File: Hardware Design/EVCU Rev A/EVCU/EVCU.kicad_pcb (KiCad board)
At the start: 4 copper layers, 60 parts, among them J1 Conn_01x06, J4 Micro_SD_Card, U1 AZ1084-3.3, U10 EMIF06-MSD02N16, U11 ESDALC6V1W5, U2 AP62250WU-7, U3 STM32L4R9ZITx, U5 MPU-6500, U6 SN65HVD230, U9 ESDCAN24-2BLY, X1 ECS-2520MV-160-CN-TR

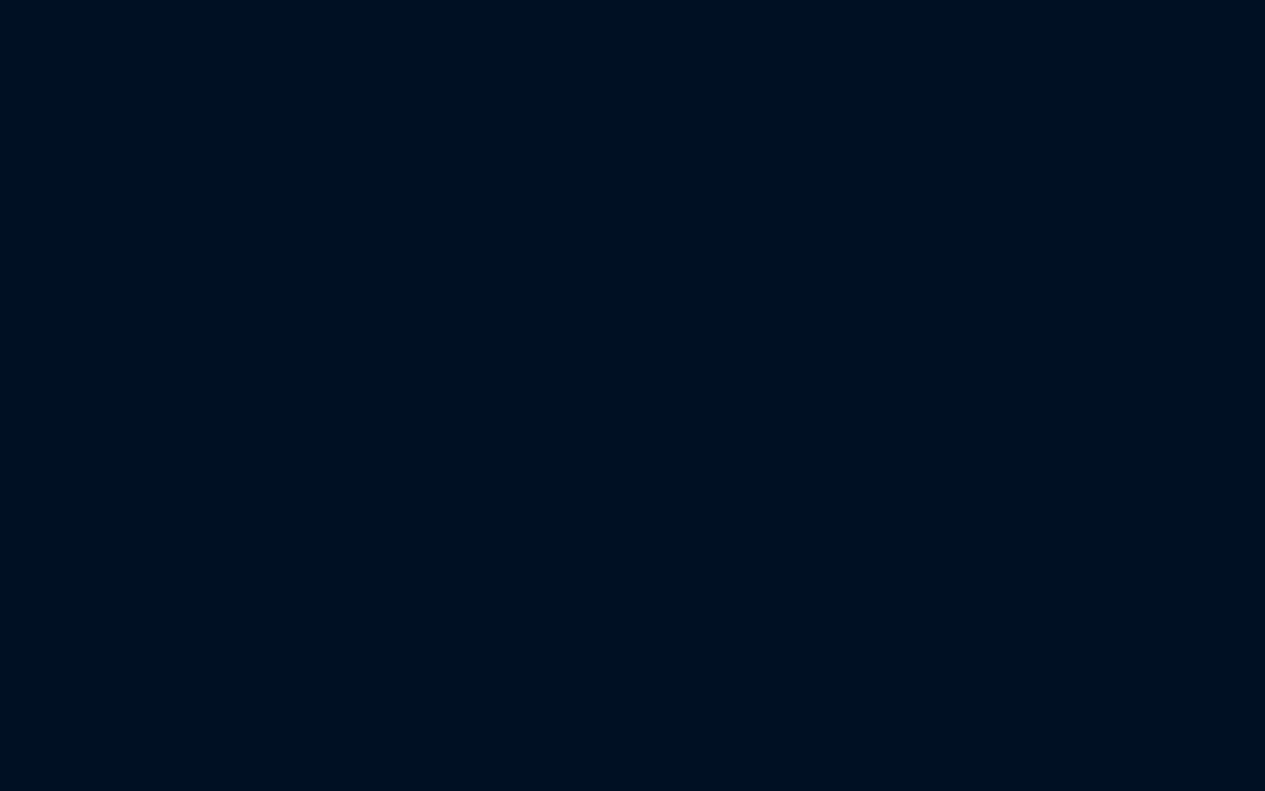
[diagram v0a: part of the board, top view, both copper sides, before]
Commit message: cap 1206 change, fuse, lin reg to 1117, testpoints, bom additions
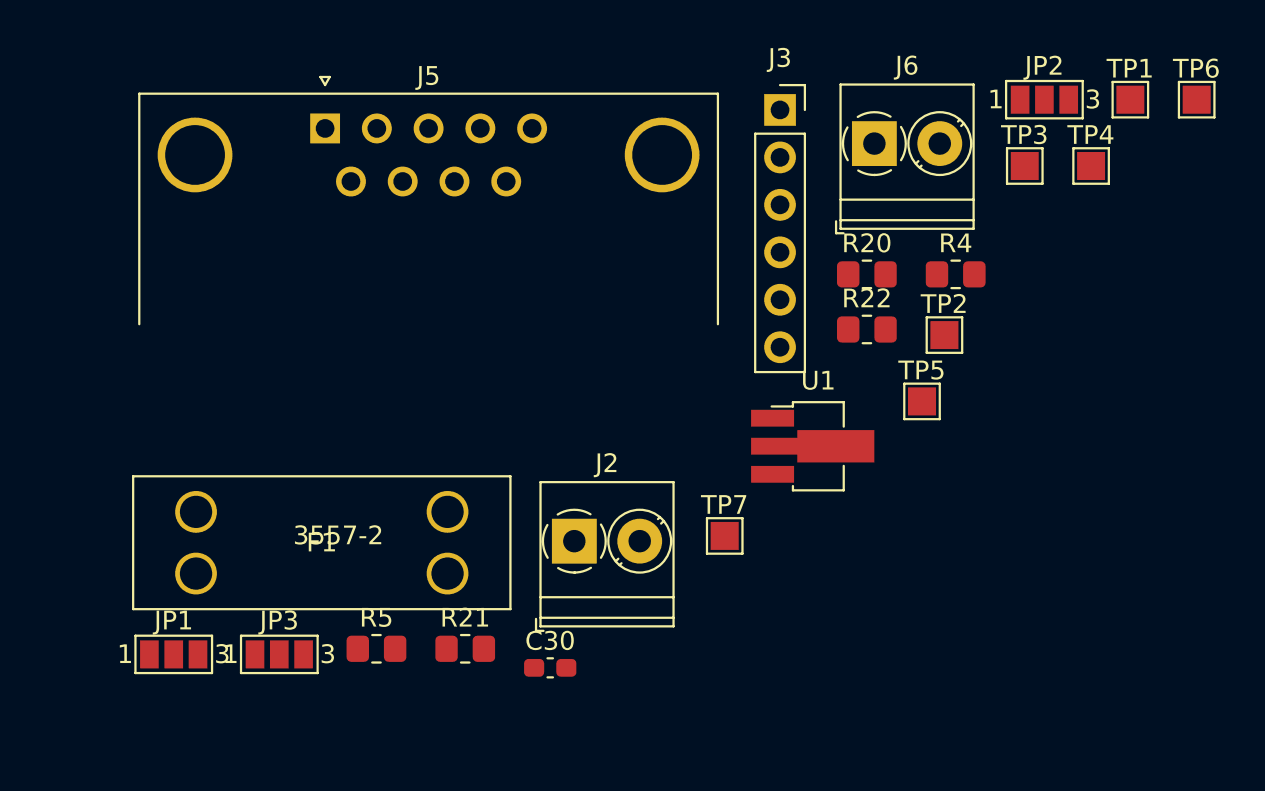
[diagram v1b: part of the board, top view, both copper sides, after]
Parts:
- added C30: 0.1uF, Capacitor_SMD:C_0603_1608Metric_Pad1.08x0.95mm_HandSolder, F.Cu at (188.3, 92.4)
- added F1: 3557-2, 3557-2:3557-2, F.Cu at (169.4, 84.1)
- added J2: Conn_01x02, TerminalBlock_Phoenix:TerminalBlock_Phoenix_PT-1,5-2-3.5-H_1x02_P3.50mm_Horizontal, F.Cu at (189.6, 85.6)
- added J3: APPS/BSE_Conn, Connector_PinSocket_2.54mm:PinSocket_1x06_P2.54mm_Vertical, F.Cu at (200.6, 62.5)
- added J5: DB9_Male, Connector_Dsub:DSUB-9_Male_Horizontal_P2.77x2.84mm_EdgePinOffset7.70mm_Housed_MountingHolesOffset9.12mm, F.Cu at (176.3, 63.5)
- added J6: Conn_01x02, TerminalBlock_Phoenix:TerminalBlock_Phoenix_PT-1,5-2-3.5-H_1x02_P3.50mm_Horizontal, F.Cu at (205.7, 64.3)
- added JP1: SolderJumper_3_Open, Jumper:SolderJumper-3_P1.3mm_Open_Pad1.0x1.5mm_NumberLabels, F.Cu at (168.2, 91.7)
- added JP2: SolderJumper_3_Open, Jumper:SolderJumper-3_P1.3mm_Open_Pad1.0x1.5mm_NumberLabels, F.Cu at (214.8, 62.0)
- added JP3: SolderJumper_3_Open, Jumper:SolderJumper-3_P1.3mm_Open_Pad1.0x1.5mm_NumberLabels, F.Cu at (173.8, 91.7)
- added R20: 34kR, Resistor_SMD:R_0805_2012Metric_Pad1.20x1.40mm_HandSolder, F.Cu at (205.3, 71.3)
- added R21: 100kR, Resistor_SMD:R_0805_2012Metric_Pad1.20x1.40mm_HandSolder, F.Cu at (183.8, 91.4)
- added R22: 100kR, Resistor_SMD:R_0805_2012Metric_Pad1.20x1.40mm_HandSolder, F.Cu at (205.3, 74.3)
- added R4: 100kR, Resistor_SMD:R_0805_2012Metric_Pad1.20x1.40mm_HandSolder, F.Cu at (210.0, 71.3)
- added R5: 33kR, Resistor_SMD:R_0805_2012Metric_Pad1.20x1.40mm_HandSolder, F.Cu at (179.0, 91.4)
- added TP1: TestPoint_Probe, TestPoint:TestPoint_Pad_1.5x1.5mm, F.Cu at (219.4, 62.0)
- added TP2: TestPoint_Probe, TestPoint:TestPoint_Pad_1.5x1.5mm, F.Cu at (209.4, 74.6)
- added TP3: TestPoint_Probe, TestPoint:TestPoint_Pad_1.5x1.5mm, F.Cu at (213.7, 65.5)
- added TP4: TestPoint_Probe, TestPoint:TestPoint_Pad_1.5x1.5mm, F.Cu at (217.3, 65.5)
- added TP5: TestPoint_Probe, TestPoint:TestPoint_Pad_1.5x1.5mm, F.Cu at (208.2, 78.1)
- added TP6: TestPoint_Probe, TestPoint:TestPoint_Pad_1.5x1.5mm, F.Cu at (222.9, 62.0)
- added TP7: TestPoint_Probe, TestPoint:TestPoint_Pad_1.5x1.5mm, F.Cu at (197.7, 85.3)
- added U1: AZ1117-3.3, Package_TO_SOT_SMD:SOT-89-3_Handsoldering, F.Cu at (202.4, 80.5)
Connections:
- C25 pad 1: /VOUT_1_APPS -> Net-(C25-Pad1)
- C26 pad 1: /VOUT_2_APPS -> Net-(C26-Pad1)
- R8 pad 1: /VOUT_1_APPS -> Net-(C25-Pad1)
- R9 pad 1: /VOUT_2_APPS -> Net-(C26-Pad1)
- U2 pad 5: unconnected-(U2-Pad5) -> +BATT
- U3 pad 108: unconnected-(U3-Pad108) -> +3V3
- U3 pad 33: unconnected-(U3-Pad33) -> /VOUT_BSE

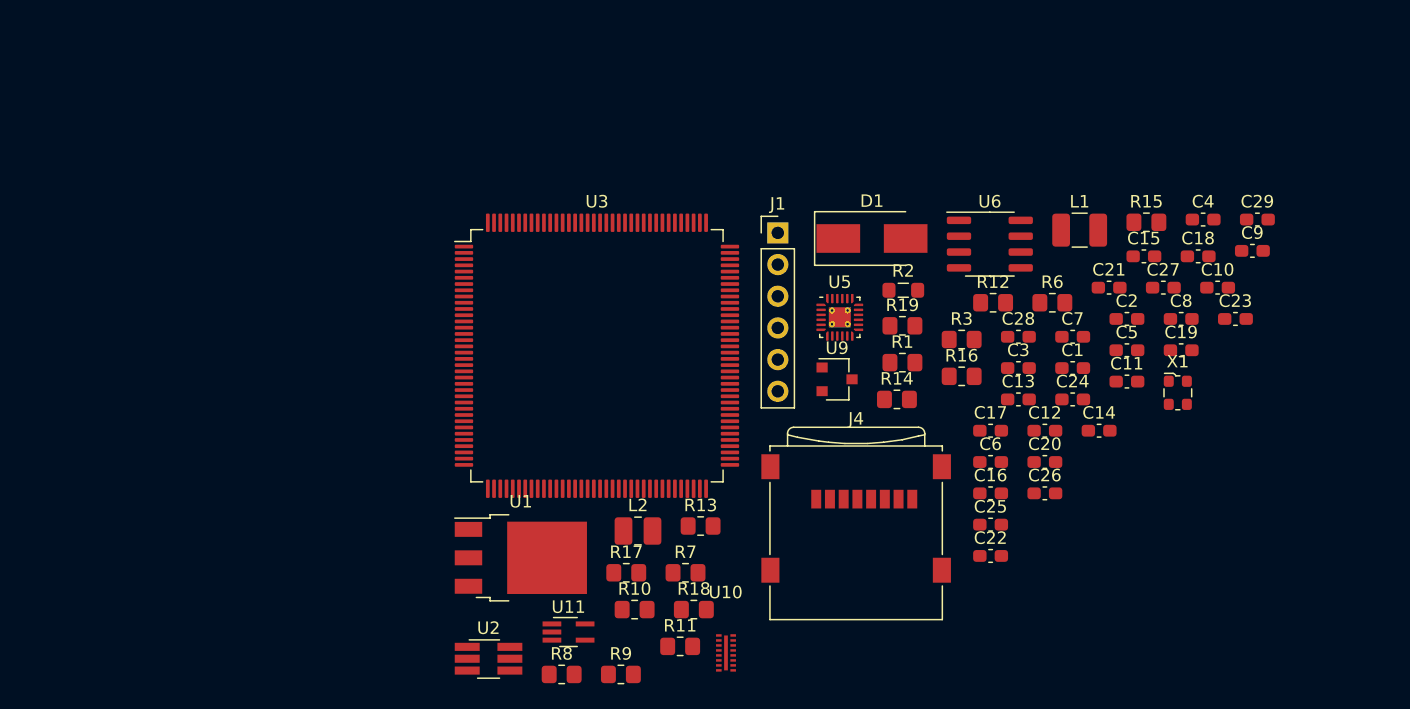
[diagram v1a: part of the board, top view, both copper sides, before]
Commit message: accelerometer layout and op-amp footprint
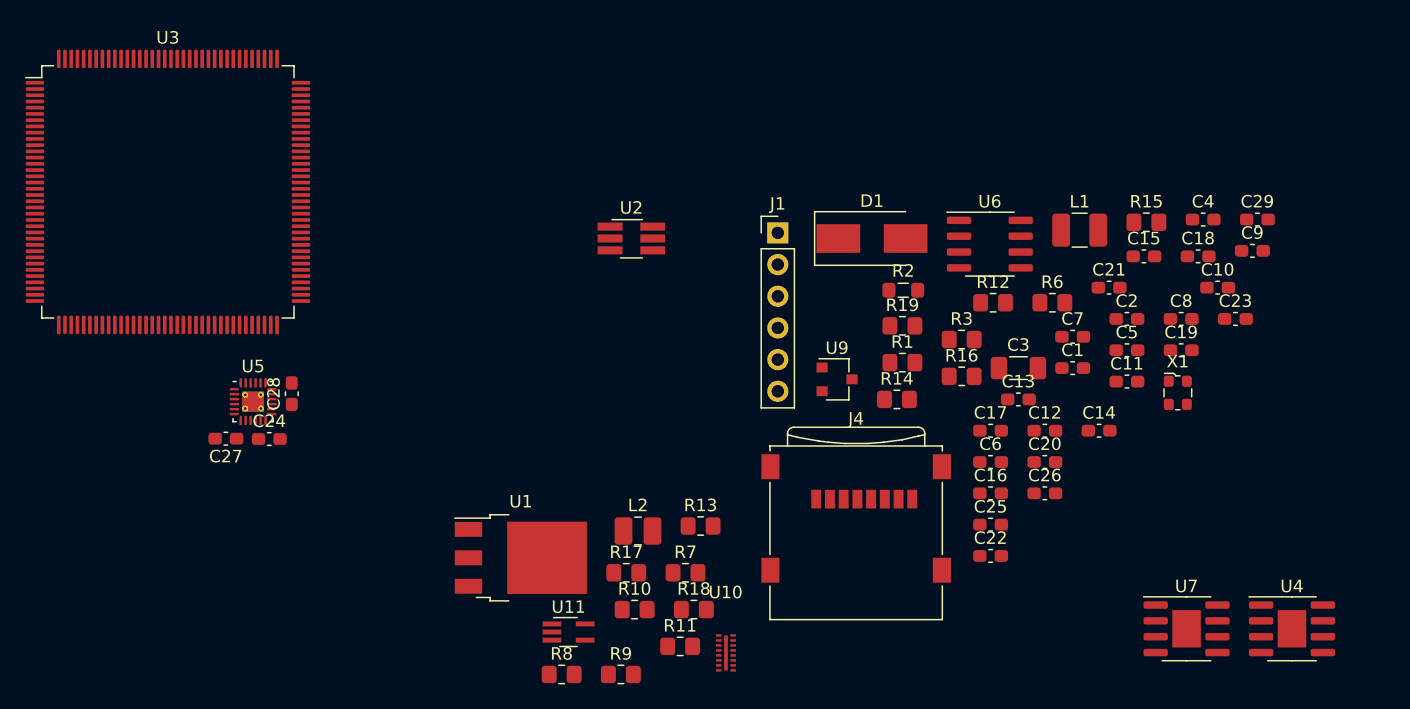
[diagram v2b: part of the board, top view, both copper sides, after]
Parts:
- added U4: LM358, Package_SO:SOIC-8-1EP_3.9x4.9mm_P1.27mm_EP2.29x3mm, F.Cu at (147.3, 94.0)
- added U7: LM358, Package_SO:SOIC-8-1EP_3.9x4.9mm_P1.27mm_EP2.29x3mm, F.Cu at (138.9, 94.0)
- C3: footprint Capacitor_SMD:C_0603_1608Metric_Pad1.08x0.95mm_HandSolder -> Capacitor_SMD:C_1206_3216Metric_Pad1.33x1.80mm_HandSolder
- moved C27 76.1 mm to (61.8, 78.7), turned to 180 degrees
- moved C24 64.5 mm to (65.3, 78.8)
- moved C28 58.4 mm to (67.1, 75.1), turned to 90 degrees
- moved U5 47.5 mm to (64.0, 75.8)
- moved U3 36.8 mm to (57.2, 59.0)
- moved U2 35.6 mm to (94.4, 62.7)

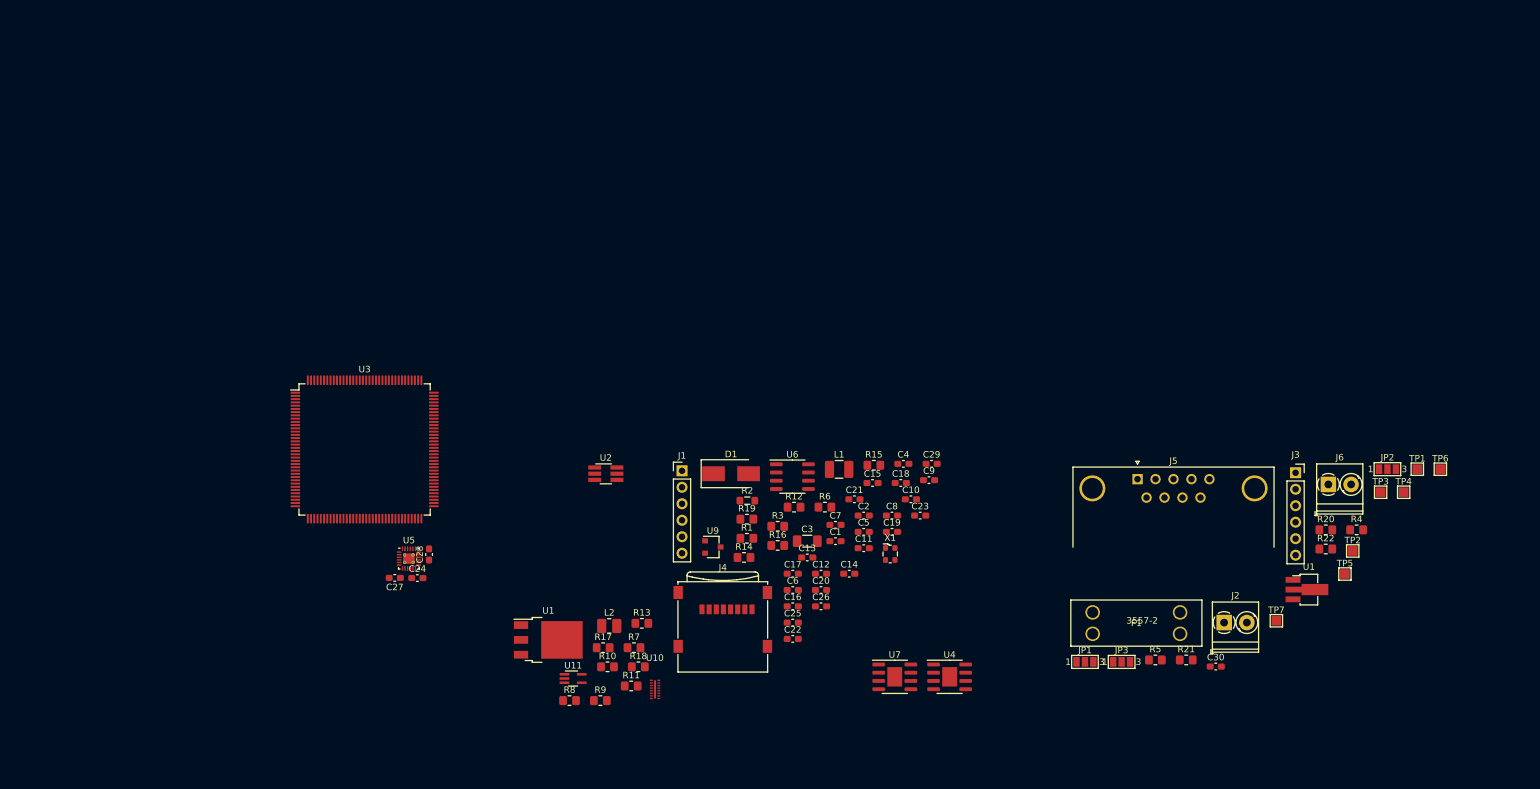
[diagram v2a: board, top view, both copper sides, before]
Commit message: dcdc and filter layout
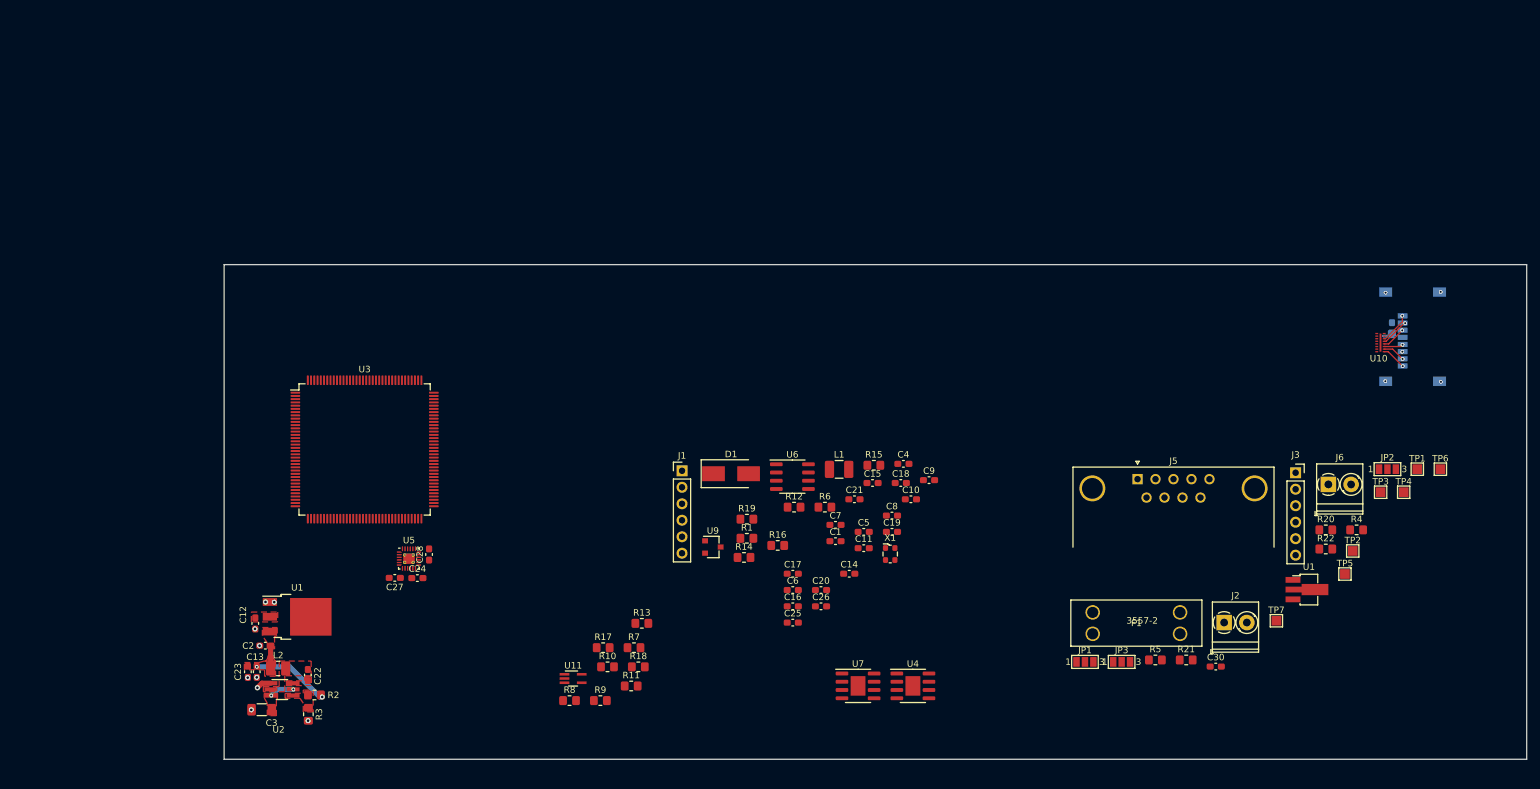
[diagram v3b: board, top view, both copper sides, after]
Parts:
- C29, J4: moved to B.Cu
- R2: footprint Inductor_SMD:L_0805_2012Metric_Pad1.05x1.20mm_HandSolder -> Resistor_SMD:R_0805_2012Metric_Pad1.20x1.40mm_HandSolder
- moved U10 123.9 mm to (213.7, 42.4)
- moved J4 114.8 mm to (218.6, 41.6), turned to -90 degrees
- moved C23 106.3 mm to (39.2, 93.2), turned to -90 degrees
- moved C2 94.3 mm to (41.9, 89.2), turned to 180 degrees
- moved C3 88.0 mm to (41.3, 99.0), turned to 180 degrees
- moved C12 87.5 mm to (40.4, 85.8), turned to -90 degrees
- moved C13 86.6 mm to (40.6, 93.2), turned to -90 degrees
- moved R3 77.9 mm to (48.5, 99.7), turned to -90 degrees
- moved C22 74.9 mm to (48.5, 93.7), turned to 90 degrees
- moved C29 73.9 mm to (215.5, 40.3), turned to -90 degrees
- moved R2 73.1 mm to (49.5, 96.8), turned to 180 degrees
- moved U2 59.9 mm to (44.5, 95.9)
- moved L2 51.4 mm to (43.9, 92.7), turned to 180 degrees
- moved U1 38.9 mm to (46.8, 84.7)
- moved U4 5.82 mm to (141.7, 95.4)
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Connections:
- net Net-(C22-Pad1) renamed /BST
- net Net-(C22-Pad2) renamed /SW
- net Net-(R2-Pad2) renamed /FB
- U4 pad 5: unconnected-(U4-Pad5) -> /LMB+
- U4 pad 6: unconnected-(U4-Pad6) -> /LMB-
- U4 pad 7: unconnected-(U4-Pad7) -> /LMBOUT
- U7 pad 5: /LMB+ -> unconnected-(U7-Pad5)
- U7 pad 6: /LMB- -> unconnected-(U7-Pad6)
- U7 pad 7: /LMBOUT -> unconnected-(U7-Pad7)
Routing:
- net +5V: track 0.00 -> 15.5 mm, vias 0 -> 2
- net /FILTER_DAT2: track 0.00 -> 4.81 mm, vias 0 -> 1
- net /FILTER_DAT3: track 0.00 -> 4.39 mm, vias 0 -> 1
- net +BATT: track 0.00 -> 3.79 mm, vias 0 -> 2
- net /FILTER_DAT1: track 0.00 -> 3.77 mm, vias 0 -> 1
- net /FILTER_CMD: track 0.00 -> 3.63 mm, vias 0 -> 1
- net /FILTER_DAT0: track 0.00 -> 3.45 mm, vias 0 -> 1
- net /FILTER_CLK: track 0.00 -> 2.93 mm, vias 0 -> 1
- net GND: track 0.00 -> 2.37 mm, vias 0 -> 14
- added copper zone on B.Cu, net +3V3
- added copper zone on F.Cu, net +3V3
- added copper zone on F.Cu, net +5V
- added copper zone on F.Cu, net +BATT
- added copper zone on F.Cu, net /BST
- added copper zone on F.Cu, net /FB
- added copper zone on F.Cu, net /SW
- added copper zone on In1.Cu, net GND
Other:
- board outline added: 200.7 x 76.2 mm

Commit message: PCB layout for 1st iteration done, some labelling required
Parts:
- removed the U1 at (202.4, 80.5)
- removed the U1 at (46.8, 84.7)
- added C31: 100nF, Capacitor_SMD:C_0603_1608Metric_Pad1.08x0.95mm_HandSolder, B.Cu at (49.4, 50.0)
- added U1: AZ1117-3.3, Package_TO_SOT_SMD:SOT-89-3_Handsoldering, F.Cu at (47.2, 86.9)
- C1, C10, C11, C14, C15, C16, C17, C18, C19, C21, C4, C5, C6, C7, C8, C9, L1, R13, R14, R15, R16, R19, R20, R21, U9: moved to B.Cu
- J4: moved to F.Cu
- moved TP6 190.2 mm to (34.4, 87.1), turned to -90 degrees
- moved J3 183.9 mm to (18.8, 90.2), turned to 180 degrees
- moved JP2 181.5 mm to (34.5, 82.3), turned to -90 degrees
- moved TP5 180.5 mm to (28.2, 65.0), turned to -90 degrees
- moved R20 177.0 mm to (29.6, 92.9), turned to 180 degrees
- moved R4 176.7 mm to (34.6, 92.9), turned to 180 degrees
- moved R22 176.6 mm to (29.3, 89.8), turned to 90 degrees
- moved TP1 176.1 mm to (46.7, 96.8)
- moved TP2 157.5 mm to (52.4, 87.1)
- moved TP7 156.0 mm to (41.8, 92.7), turned to -90 degrees
- moved R21 153.3 mm to (30.5, 90.2), turned to 90 degrees
- moved C30 152.7 mm to (35.7, 90.3), turned to 90 degrees
- moved U10 147.4 mm to (66.4, 37.7)
- moved R5 147.1 mm to (32.0, 90.7), turned to 180 degrees
- moved C29 146.4 mm to (69.1, 36.4), turned to 180 degrees
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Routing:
- net GND: track 2.37 -> 82.3 mm, vias 14 -> 65
- net +3V3: track 0.00 -> 59.3 mm, vias 0 -> 29
- net /NRST: track 0.00 -> 49.6 mm, vias 0 -> 1
- net /CAN_H: track 0.00 -> 43.1 mm, vias 0 -> 1
- net /SWCLK: track 0.00 -> 39.2 mm, vias 0 -> 2
- net /CAN_L: track 0.00 -> 35.5 mm, vias 0 -> 2
- net +5V: track 15.5 -> 50.6 mm, vias 2 -> 3
- net /SWDIO: track 0.00 -> 32.4 mm, vias 0 -> 2
- net /VOUT_BSE: track 0.00 -> 27.8 mm
- net /CAN_TX: track 0.00 -> 26.9 mm
- net /CAN_RX: track 0.00 -> 25.5 mm
- net /MCU_CD: track 0.00 -> 25.1 mm, vias 0 -> 2
- net /VOUT_2_APPS: track 0.00 -> 21.9 mm
- net /MCU_DAT1: track 0.00 -> 17.5 mm, vias 0 -> 2
- net /MCU_DAT0: track 0.00 -> 17.2 mm
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- added copper zone on B.Cu, net +3.3VA
- added copper zone on In2.Cu, net +3V3
- added copper zone on F.Cu, net /CAN_Rs
- added copper zone on F.Cu, net /CAN_Vref
- added copper zone on F.Cu, net /LMA+
- added copper zone on F.Cu, net /LMA+_BSE
- added copper zone on B.Cu, net /LMA-
- added copper zone on B.Cu, net /LMA-_BSE
- added copper zone on F.Cu, net /LMAOUT
- added copper zone on F.Cu, net /LMAOUT_BSE
- added copper zone on F.Cu, net /LMB+
- added copper zone on B.Cu, net /LMB-
- added copper zone on F.Cu, net /LMBOUT
- added copper zone on F.Cu, net Net-(C25-Pad1)
- added copper zone on F.Cu, net Net-(C26-Pad1)
- added copper zone on F.Cu, net Net-(C30-Pad1)
- added copper zone on F.Cu, net Net-(F1-Pad)
- removed copper zone on B.Cu, net +3V3
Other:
- board size 200.7 x 76.2 mm -> 119.4 x 76.4 mm
- board text added: "VREF+ capacitors,F1 needs to be fixed Labeling test points, SW debug etc Will have to be relaid for more customisability"

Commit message: ur mom
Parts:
- added H1: MountingHole, MountingHole:MountingHole_2.1mm, F.Cu at (16.9, 32.8)
- added H2: MountingHole, MountingHole:MountingHole_2.1mm, F.Cu at (16.5, 103.4)
- added H3: MountingHole, MountingHole:MountingHole_2.1mm, F.Cu at (131.6, 67.3)
- added H4: MountingHole, MountingHole:MountingHole_2.1mm, F.Cu at (131.6, 103.6)
- added Q1: Q_PMOS_GSD, Package_TO_SOT_SMD:SOT-23, F.Cu at (76.5, 101.6)
- U5: footprint Package_DFN_QFN:QFN-24-1EP_3x3mm_P0.4mm_EP1.75x1.6mm_ThermalVias -> Package_DFN_QFN:QFN-24-3x3mm_P0.4mm_EP1.75x1.6mm
- moved J2 4.65 mm to (82.1, 100.9)
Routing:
- net GND: track 82.3 -> 83.4 mm, vias 65 -> 66
- added copper zone on F.Cu, net Net-(F1-Pad)
